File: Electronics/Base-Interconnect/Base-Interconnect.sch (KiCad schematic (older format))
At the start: 4 parts

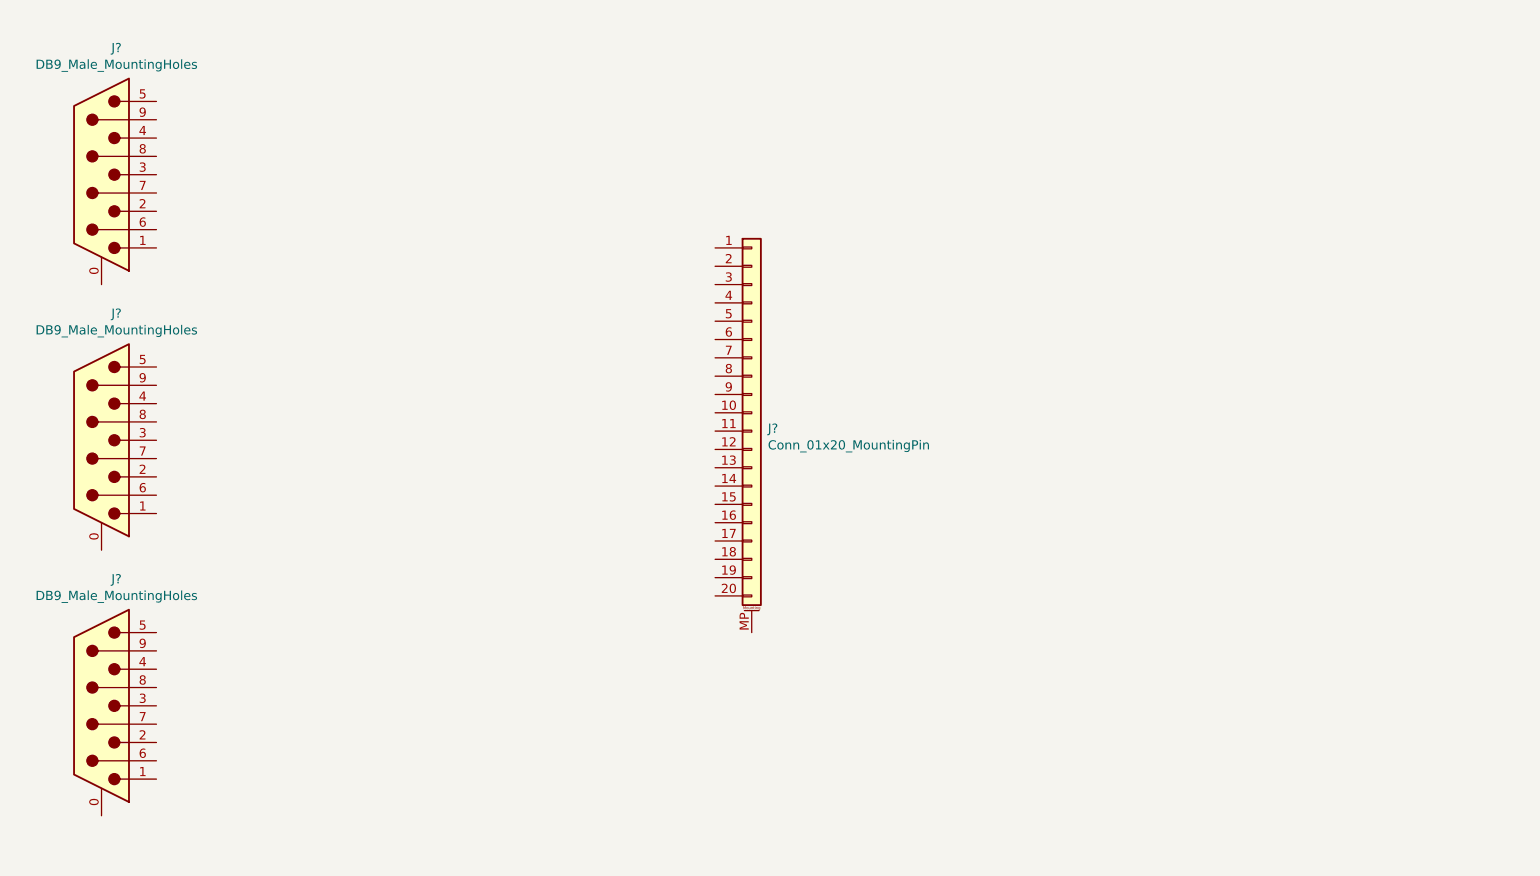
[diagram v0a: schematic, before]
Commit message: Base interconnect and head interconnect in fabrication
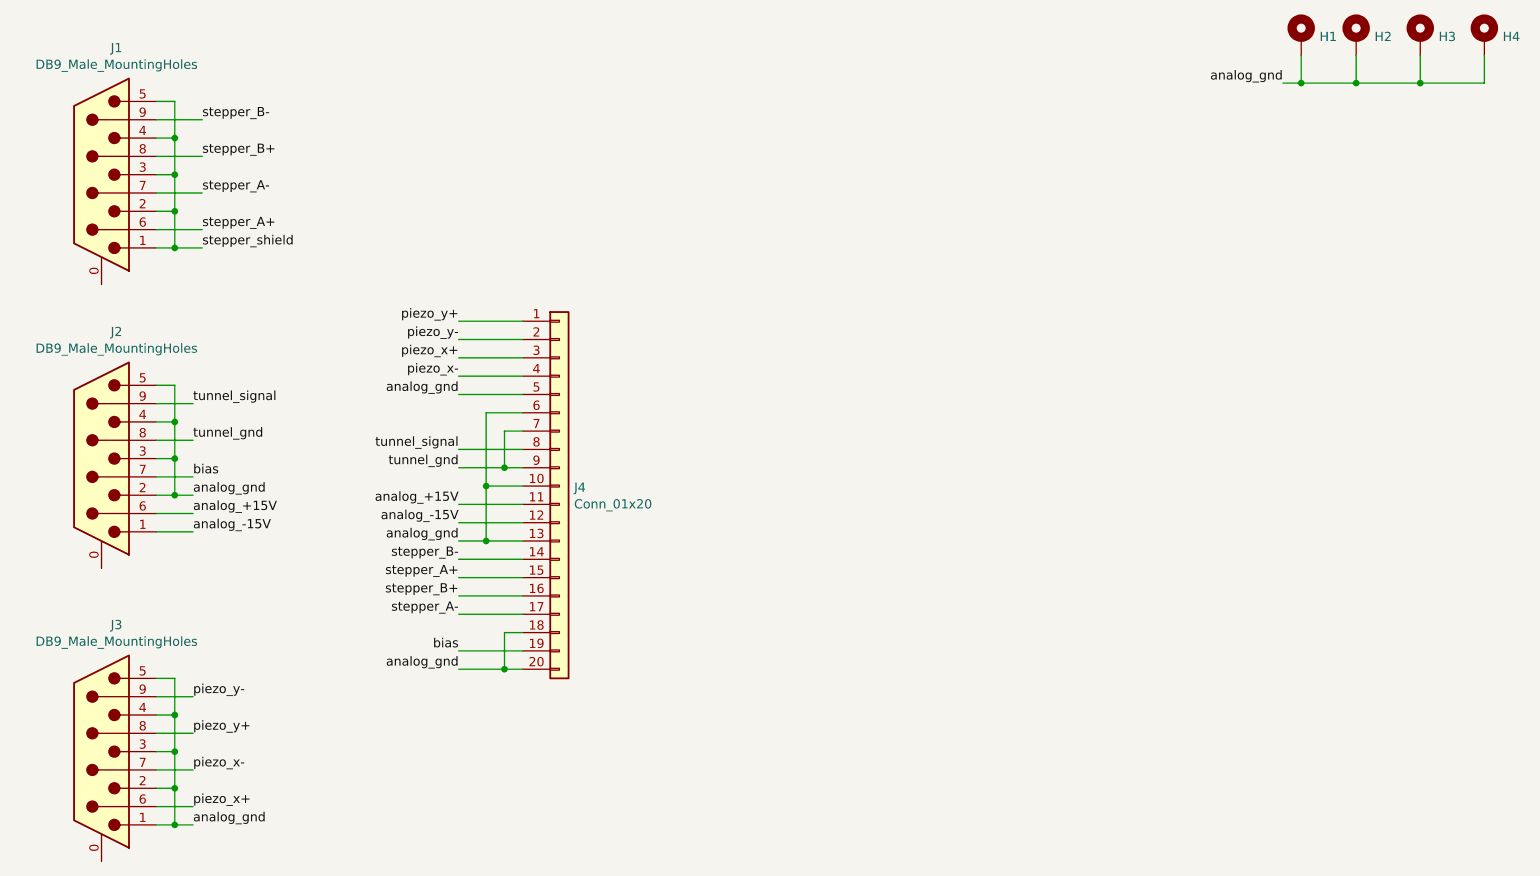
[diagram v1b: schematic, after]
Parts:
- removed J? (x2): DB9_Male_MountingHoles, STM_Custom_Lib:DSUB-9_Amphenol_LD09S33E4GV00LF, symbol Connector:DB9_Male_MountingHoles
- removed J?: Conn_01x20_MountingPin, Connector_FFC-FPC:TE_2-84953-0_1x20-1MP_P1.0mm_Horizontal, symbol Connector_Generic_MountingPin:Conn_01x20_MountingPin
- added H1, H2, H3, H4: MountingHole_Pad, MountingHole:MountingHole_3.2mm_M3_Pad_Via, symbol Mechanical:MountingHole_Pad
- added J2, J3: DB9_Male_MountingHoles, STM_Custom_Lib:DSUB-9_Amphenol_LD09S33E4GV00LF-Center, symbol Connector:DB9_Male_MountingHoles
- added J4: Conn_01x20, STM_Custom_Lib:molex_0526102072, symbol Connector_Generic:Conn_01x20
- J1: renamed from J?; footprint STM_Custom_Lib:DSUB-9_Amphenol_LD09S33E4GV00LF -> STM_Custom_Lib:DSUB-9_Amphenol_LD09S33E4GV00LF-Center
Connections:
- net stepper_shield: now reaches J1.1
- net stepper_shield: now also J1.2, J1.3, J1.4, J1.5
- net stepper_A+: now reaches J1.6
- net stepper_A+: now also J4.15 (Pin_15)
- net stepper_A-: now reaches J1.7
- net stepper_A-: now also J4.17 (Pin_17)
- net stepper_B+: now reaches J1.8
- net stepper_B+: now also J4.16 (Pin_16)
- net stepper_B-: now reaches J1.9
- net stepper_B-: now also J4.14 (Pin_14)
- new net analog_+15V: J2.6, J4.11 (Pin_11)
- new net analog_-15V: J2.1, J4.12 (Pin_12)
- new net analog_gnd: H1.1, H2.1, H3.1, H4.1, J2.2, J2.3, J2.4, J2.5, J3.1, J3.2, J3.3, J3.4, J3.5, J4.10 (Pin_10), J4.13 (Pin_13), J4.18 (Pin_18), J4.20 (Pin_20), J4.5 (Pin_5), J4.6 (Pin_6)
- new net bias: J2.7, J4.19 (Pin_19)
- new net piezo_x+: J3.6, J4.3 (Pin_3)
- new net piezo_x-: J3.7, J4.4 (Pin_4)
- new net piezo_y+: J3.8, J4.1 (Pin_1)
- new net piezo_y-: J3.9, J4.2 (Pin_2)
- new net tunnel_gnd: J2.8, J4.7 (Pin_7), J4.9 (Pin_9)
- new net tunnel_signal: J2.9, J4.8 (Pin_8)

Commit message: Added images
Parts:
- J1, J2, J3: Digikey (none) -> 609-5186-ND; Reichelt (none) -> RND 205-00770
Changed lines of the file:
@@
 F 2 "STM_Custom_Lib:DSUB-9_Amphenol_LD09S33E4GV00LF-Center" H 2450 2100 50  0001 C CNN
 F 3 " ~" H 2450 2100 50  0001 C CNN
+F 4 "609-5186-ND" H 2450 2100 50  0001 C CNN "Digikey"
+F 5 "RND 205-00770" H 2450 2100 50  0001 C CNN "Reichelt"
 	1    2450 2100
 	-1   0    0    -1
@@
 F 2 "STM_Custom_Lib:DSUB-9_Amphenol_LD09S33E4GV00LF-Center" H 2450 3650 50  0001 C CNN
 F 3 " ~" H 2450 3650 50  0001 C CNN
+F 4 "609-5186-ND" H 2450 3650 50  0001 C CNN "Digikey"
+F 5 "RND 205-00770" H 2450 3650 50  0001 C CNN "Reichelt"
 	1    2450 3650
 	-1   0    0    -1
@@
 F 2 "STM_Custom_Lib:DSUB-9_Amphenol_LD09S33E4GV00LF-Center" H 2450 5250 50  0001 C CNN
 F 3 " ~" H 2450 5250 50  0001 C CNN
+F 4 "609-5186-ND" H 2450 5250 50  0001 C CNN "Digikey"
+F 5 "RND 205-00770" H 2450 5250 50  0001 C CNN "Reichelt"
 	1    2450 5250
 	-1   0    0    -1

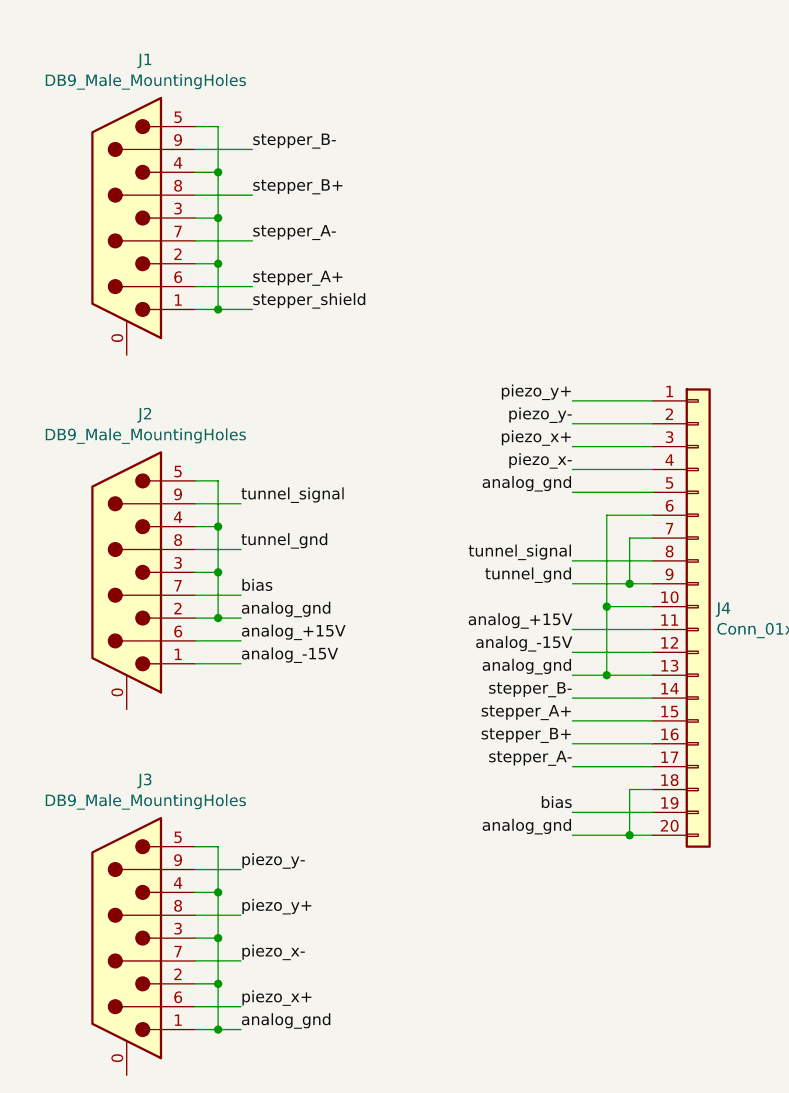
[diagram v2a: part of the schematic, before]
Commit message: Added sample-bias interconnect and base interconnect V2
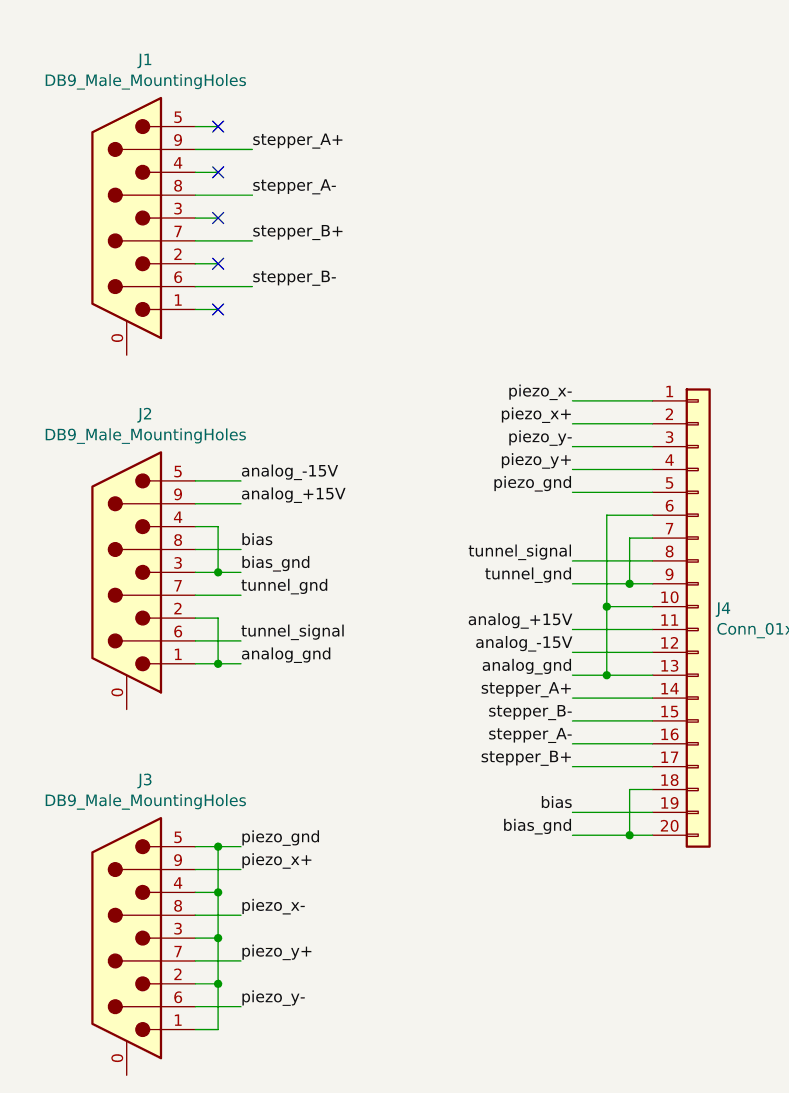
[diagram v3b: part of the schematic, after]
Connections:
- net analog_+15V: now also J2.9; no longer J2.6
- net analog_-15V: now also J2.5; no longer J2.1
- net analog_gnd: now also J2.1; no longer J2.3, J2.4, J2.5, J3.1, J3.2, J3.3, J3.4, J3.5, J4.18 (Pin_18), J4.20 (Pin_20), J4.5 (Pin_5)
- net bias: now also J2.8; no longer J2.7
- net piezo_x+: now also J3.9, J4.2 (Pin_2); no longer J3.6, J4.3 (Pin_3)
- net piezo_x-: now also J3.8, J4.1 (Pin_1); no longer J3.7, J4.4 (Pin_4)
- net piezo_y+: now also J3.7, J4.4 (Pin_4); no longer J3.8, J4.1 (Pin_1)
- net piezo_y-: now also J3.6, J4.3 (Pin_3); no longer J3.9, J4.2 (Pin_2)
- net stepper_A+: now also J1.9, J4.14 (Pin_14); no longer J1.6, J4.15 (Pin_15)
- net stepper_A-: now also J1.8, J4.16 (Pin_16); no longer J1.7, J4.17 (Pin_17)
- net stepper_B+: now also J1.7, J4.17 (Pin_17); no longer J1.8, J4.16 (Pin_16)
- net stepper_B-: now also J1.6, J4.15 (Pin_15); no longer J1.9, J4.14 (Pin_14)
- net tunnel_gnd: now also J2.7; no longer J2.8
- net tunnel_signal: now also J2.6; no longer J2.9
- removed net stepper_shield: J1.1, J1.2, J1.3, J1.4, J1.5
- new net bias_gnd: J2.3, J2.4, J4.18 (Pin_18), J4.20 (Pin_20)
- new net piezo_gnd: J3.1, J3.2, J3.3, J3.4, J3.5, J4.5 (Pin_5)
- no-connect marks 0 -> 5
